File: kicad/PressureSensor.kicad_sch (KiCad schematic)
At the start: 1 part

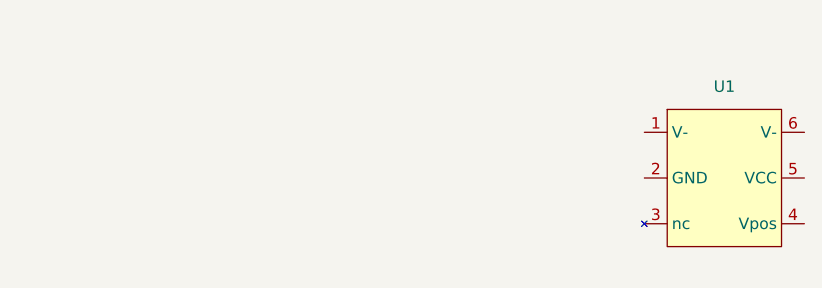
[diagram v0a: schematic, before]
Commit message: custom footprints
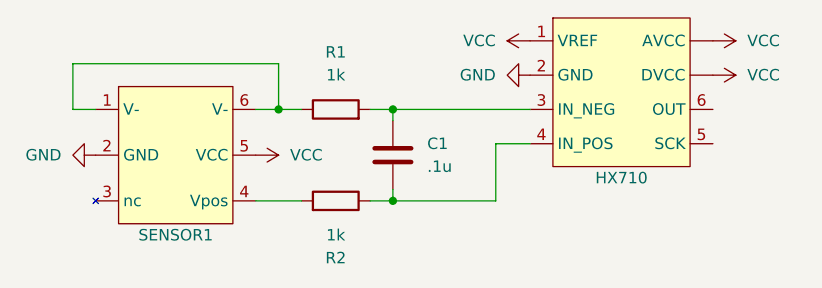
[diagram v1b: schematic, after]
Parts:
- added C1: .1u, symbol Device:C
- added HX710: ~, Package_SO:SOIC-8_5.23x5.23mm_P1.27mm, symbol New_Library:hx710
- added R1, R2: 1k, symbol Device:R
- SENSOR1: renamed from U1; footprint (none) -> Library:pressure-sensor-SOIC-6
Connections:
- net at SENSOR1.1 (V-): now also SENSOR1.6 (V-), R1.1
- net GND: now reaches SENSOR1.2 (GND)
- net GND: now also HX710.2 (GND)
- net at SENSOR1.4 (Vpos): now also R2.2
- net VCC: now reaches SENSOR1.5 (VCC)
- net VCC: now also HX710. (DVCC), HX710.1 (VREF)
- new net: C1.1, HX710.3 (IN_NEG), R1.2
- new net: C1.2, HX710.4 (IN_POS), R2.1
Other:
- moved on the sheet: SENSOR1

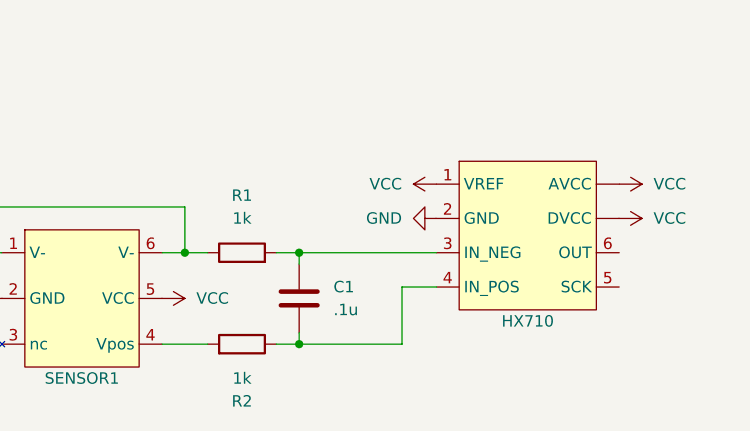
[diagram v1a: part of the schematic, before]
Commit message: schematic: improve filtering
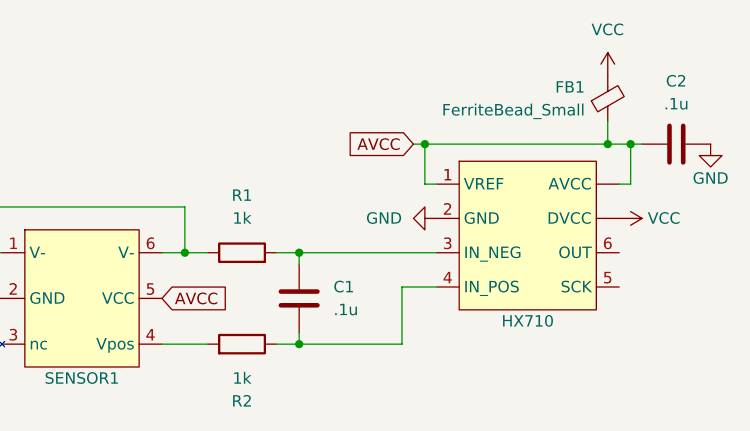
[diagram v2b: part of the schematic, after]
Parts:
- added C2: .1u, symbol Device:C
- added FB1: FerriteBead_Small, symbol Device:FerriteBead_Small
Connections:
- net GND: now also C2.2
- net VCC: now also FB1.2; no longer HX710.1 (VREF), SENSOR1.5 (VCC)
- new net AVCC: C2.1, FB1.1, HX710. (DVCC), HX710.1 (VREF), SENSOR1.5 (VCC)
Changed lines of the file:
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@@
 (kicad_sch (version 20230121) (generator eeschema)
   (paper "A4")
+  (junction (at 130.81 76.835) (diameter 0) (color 0 0 0 0)
+  )
   (junction (at 83.82 88.9) (diameter 0) (color 0 0 0 0)
   )
   (junction (at 96.52 88.9) (diameter 0) (color 0 0 0 0)
   )
+  (junction (at 110.49 76.835) (diameter 0) (color 0 0 0 0)
+  )
   (junction (at 96.52 99.06) (diameter 0) (color 0 0 0 0)
   )
+  (junction (at 133.35 76.835) (diameter 0) (color 0 0 0 0)
+  )
   (wire (pts (xy 96.52 88.9) (xy 111.76 88.9))
     (stroke (width 0) (type default))
@@
     (stroke (width 0) (type default))
   )
+  (wire (pts (xy 133.35 76.835) (xy 134.62 76.835))
+    (stroke (width 0) (type default))
+  )
+  (wire (pts (xy 130.81 74.295) (xy 130.81 76.835))
+    (stroke (width 0) (type default))
+  )
+  (wire (pts (xy 133.35 81.28) (xy 133.35 76.835))
+    (stroke (width 0) (type default))
+  )
   (wire (pts (xy 81.28 88.9) (xy 83.82 88.9))
     (stroke (width 0) (type default))
   )
+  (wire (pts (xy 130.81 76.835) (xy 110.49 76.835))
+    (stroke (width 0) (type default))
+  )
   (wire (pts (xy 96.52 90.17) (xy 96.52 88.9))
     (stroke (width 0) (type default))
@@
     (stroke (width 0) (type default))
   )
+  (wire (pts (xy 109.22 76.835) (xy 110.49 76.835))
+    (stroke (width 0) (type default))
+  )
+  (wire (pts (xy 133.35 81.28) (xy 132.08 81.28))
+    (stroke (width 0) (type default))
+  )
+  (wire (pts (xy 110.49 76.835) (xy 110.49 81.28))
+    (stroke (width 0) (type default))
+  )
   (wire (pts (xy 81.28 99.06) (xy 86.36 99.06))
     (stroke (width 0) (type default))
   )
+  (wire (pts (xy 133.35 76.835) (xy 130.81 76.835))
+    (stroke (width 0) (type default))
+  )
   (wire (pts (xy 60.96 88.9) (xy 60.96 83.82))
     (stroke (width 0) (type default))
@@
     (stroke (width 0) (type default))
   )
+  (wire (pts (xy 110.49 81.28) (xy 111.76 81.28))
+    (stroke (width 0) (type default))
+  )
   (wire (pts (xy 111.76 92.71) (xy 107.95 92.71))
     (stroke (width 0) (type default))
@@
     (stroke (width 0) (type default))
   )
-  (symbol (lib_id "power:VCC") (at 132.08 85.09 270) (unit 1)
-    (in_bom yes) (on_board yes) (dnp no) (fields_autoplaced)
-    (property "Reference" "#PWR05" (at 128.27 85.09 0)
-      (effects (font (size 1.27 1.27)) hide)
-    )
-    (property "Value" "VCC" (at 135.89 85.09 90)
-      (effects (font (size 1.27 1.27)) (justify left))
-    )
-    (property "Footprint" "" (at 132.08 85.09 0)
-      (effects (font (size 1.27 1.27)) hide)
-    )
-    (property "Datasheet" "" (at 132.08 85.09 0)
-      (effects (font (size 1.27 1.27)) hide)
-    )
-    (pin "1")
-    (instances
-      (project "PressureSensor"
-        (path "/c97cbf04-475c-40dc-8f48-12fec2eb0ee0"
-          (reference "#PWR05") (unit 1)
-        )
-      )
+  (global_label "AVCC" (shape input) (at 109.22 76.835 180) (fields_autoplaced)
+    (effects (font (size 1.27 1.27)) (justify right))
+    (property "Intersheetrefs" "${INTERSHEET_REFS}" (at 101.5176 76.835 0)
+      (effects (font (size 1.27 1.27)) (justify right) hide)
+    )
+  )
+  (global_label "AVCC" (shape input) (at 81.28 93.98 0) (fields_autoplaced)
+    (effects (font (size 1.27 1.27)) (justify left))
+    (property "Intersheetrefs" "${INTERSHEET_REFS}" (at 88.9824 93.98 0)
+      (effects (font (size 1.27 1.27)) (justify left) hide)
     )
   )
@@
     )
   )
-  (symbol (lib_id "power:VCC") (at 111.76 81.28 90) (unit 1)
-    (in_bom yes) (on_board yes) (dnp no) (fields_autoplaced)
-    (property "Reference" "#PWR06" (at 115.57 81.28 0)
-      (effects (font (size 1.27 1.27)) hide)
-    )
-    (property "Value" "VCC" (at 107.95 81.28 90)
-      (effects (font (size 1.27 1.27)) (justify left))
-    )
-    (property "Footprint" "" (at 111.76 81.28 0)
-      (effects (font (size 1.27 1.27)) hide)
-    )
-    (property "Datasheet" "" (at 111.76 81.28 0)
-      (effects (font (size 1.27 1.27)) hide)
-    )
-    (pin "1")
-    (instances
-      (project "PressureSensor"
-        (path "/c97cbf04-475c-40dc-8f48-12fec2eb0ee0"
-          (reference "#PWR06") (unit 1)
+  (symbol (lib_id "Device:C") (at 138.43 76.835 90) (unit 1)
+    (in_bom yes) (on_board yes) (dnp no) (fields_autoplaced)
+    (property "Reference" "C2" (at 138.43 69.85 90)
+      (effects (font (size 1.27 1.27)))
+    )
+    (property "Value" ".1u" (at 138.43 72.39 90)
+      (effects (font (size 1.27 1.27)))
+    )
+    (property "Footprint" "" (at 142.24 75.8698 0)
+      (effects (font (size 1.27 1.27)) hide)
+    )
+    (property "Datasheet" "~" (at 138.43 76.835 0)
+      (effects (font (size 1.27 1.27)) hide)
+    )
+    (pin "1")
+    (pin "2")
+    (instances
+      (project "PressureSensor"
+        (path "/c97cbf04-475c-40dc-8f48-12fec2eb0ee0"
+          (reference "C2") (unit 1)
         )
       )
@@
     )
   )
-  (symbol (lib_id "power:VCC") (at 132.08 81.28 270) (unit 1)
-    (in_bom yes) (on_board yes) (dnp no) (fields_autoplaced)
-    (property "Reference" "#PWR04" (at 128.27 81.28 0)
-      (effects (font (size 1.27 1.27)) hide)
-    )
-    (property "Value" "VCC" (at 135.89 81.28 90)
+  (symbol (lib_id "power:VCC") (at 130.81 69.215 0) (unit 1)
+    (in_bom yes) (on_board yes) (dnp no) (fields_autoplaced)
+    (property "Reference" "#PWR04" (at 130.81 73.025 0)
+      (effects (font (size 1.27 1.27)) hide)
+    )
+    (property "Value" "VCC" (at 130.81 64.135 0)
+      (effects (font (size 1.27 1.27)))
+    )
+    (property "Footprint" "" (at 130.81 69.215 0)
+      (effects (font (size 1.27 1.27)) hide)
+    )
+    (property "Datasheet" "" (at 130.81 69.215 0)
+      (effects (font (size 1.27 1.27)) hide)
+    )
+    (pin "1")
+    (instances
+      (project "PressureSensor"
+        (path "/c97cbf04-475c-40dc-8f48-12fec2eb0ee0"
+          (reference "#PWR04") (unit 1)
+        )
+      )
+    )
+  )
+  (symbol (lib_id "power:VCC") (at 132.08 85.09 270) (unit 1)
+    (in_bom yes) (on_board yes) (dnp no)
+    (property "Reference" "#PWR05" (at 128.27 85.09 0)
+      (effects (font (size 1.27 1.27)) hide)
+    )
+    (property "Value" "VCC" (at 135.255 85.09 90)
       (effects (font (size 1.27 1.27)) (justify left))
     )
-    (property "Footprint" "" (at 132.08 81.28 0)
-      (effects (font (size 1.27 1.27)) hide)
-    )
-    (property "Datasheet" "" (at 132.08 81.28 0)
-      (effects (font (size 1.27 1.27)) hide)
-    )
-    (pin "1")
-    (instances
-      (project "PressureSensor"
-        (path "/c97cbf04-475c-40dc-8f48-12fec2eb0ee0"
-          (reference "#PWR04") (unit 1)
+    (property "Footprint" "" (at 132.08 85.09 0)
+      (effects (font (size 1.27 1.27)) hide)
+    )
+    (property "Datasheet" "" (at 132.08 85.09 0)
+      (effects (font (size 1.27 1.27)) hide)
+    )
+    (pin "1")
+    (instances
+      (project "PressureSensor"
+        (path "/c97cbf04-475c-40dc-8f48-12fec2eb0ee0"
+          (reference "#PWR05") (unit 1)
+        )
+      )
+    )
+  )
+  (symbol (lib_id "Device:FerriteBead_Small") (at 130.81 71.755 0) (mirror x) (unit 1)
+    (in_bom yes) (on_board yes) (dnp no)
+    (property "Reference" "FB1" (at 128.27 70.5231 0)
+      (effects (font (size 1.27 1.27)) (justify right))
+    )
+    (property "Value" "FerriteBead_Small" (at 128.27 73.0631 0)
+      (effects (font (size 1.27 1.27)) (justify right))
+    )
+    (property "Footprint" "" (at 129.032 71.755 90)
+      (effects (font (size 1.27 1.27)) hide)
+    )
+    (property "Datasheet" "~" (at 130.81 71.755 0)
+      (effects (font (size 1.27 1.27)) hide)
+    )
+    (pin "1")
+    (pin "2")
+    (instances
+      (project "PressureSensor"
+        (path "/c97cbf04-475c-40dc-8f48-12fec2eb0ee0"
+          (reference "FB1") (unit 1)
         )
       )
@@
         (path "/c97cbf04-475c-40dc-8f48-12fec2eb0ee0"
           (reference "R1") (unit 1)
+        )
+      )
+    )
+  )
+  (symbol (lib_id "power:GND") (at 142.24 76.835 0) (unit 1)
+    (in_bom yes) (on_board yes) (dnp no)
+    (property "Reference" "#PWR07" (at 142.24 83.185 0)
+      (effects (font (size 1.27 1.27)) hide)
+    )
+    (property "Value" "GND" (at 142.24 80.645 0)
+      (effects (font (size 1.27 1.27)))
+    )
+    (property "Footprint" "" (at 142.24 76.835 0)
+      (effects (font (size 1.27 1.27)) hide)
+    )
+    (property "Datasheet" "" (at 142.24 76.835 0)
+      (effects (font (size 1.27 1.27)) hide)
+    )
+    (pin "1")
+    (instances
+      (project "PressureSensor"
+        (path "/c97cbf04-475c-40dc-8f48-12fec2eb0ee0"
+          (reference "#PWR07") (unit 1)
         )
       )
@@
         )
       )
-    )
-  )
-  (symbol (lib_id "power:VCC") (at 81.28 93.98 270) (unit 1)
-    (in_bom yes) (on_board yes) (dnp no) (fields_autoplaced)
-    (property "Reference" "#PWR02" (at 77.47 93.98 0)
-      (effects (font (size 1.27 1.27)) hide)
-    )
-    (property "Value" "VCC" (at 85.09 93.98 90)
-      (effects (font (size 1.27 1.27)) (justify left))
-    )
-    (property "Footprint" "" (at 81.28 93.98 0)
-      (effects (font (size 1.27 1.27)) hide)
-    )
-    (property "Datasheet" "" (at 81.28 93.98 0)
-      (effects (font (size 1.27 1.27)) hide)
-    )
-    (pin "1")
-    (instances
-      (project "PressureSensor"
-        (path "/c97cbf04-475c-40dc-8f48-12fec2eb0ee0"
-          (reference "#PWR02") (unit 1)
-        )
-      )

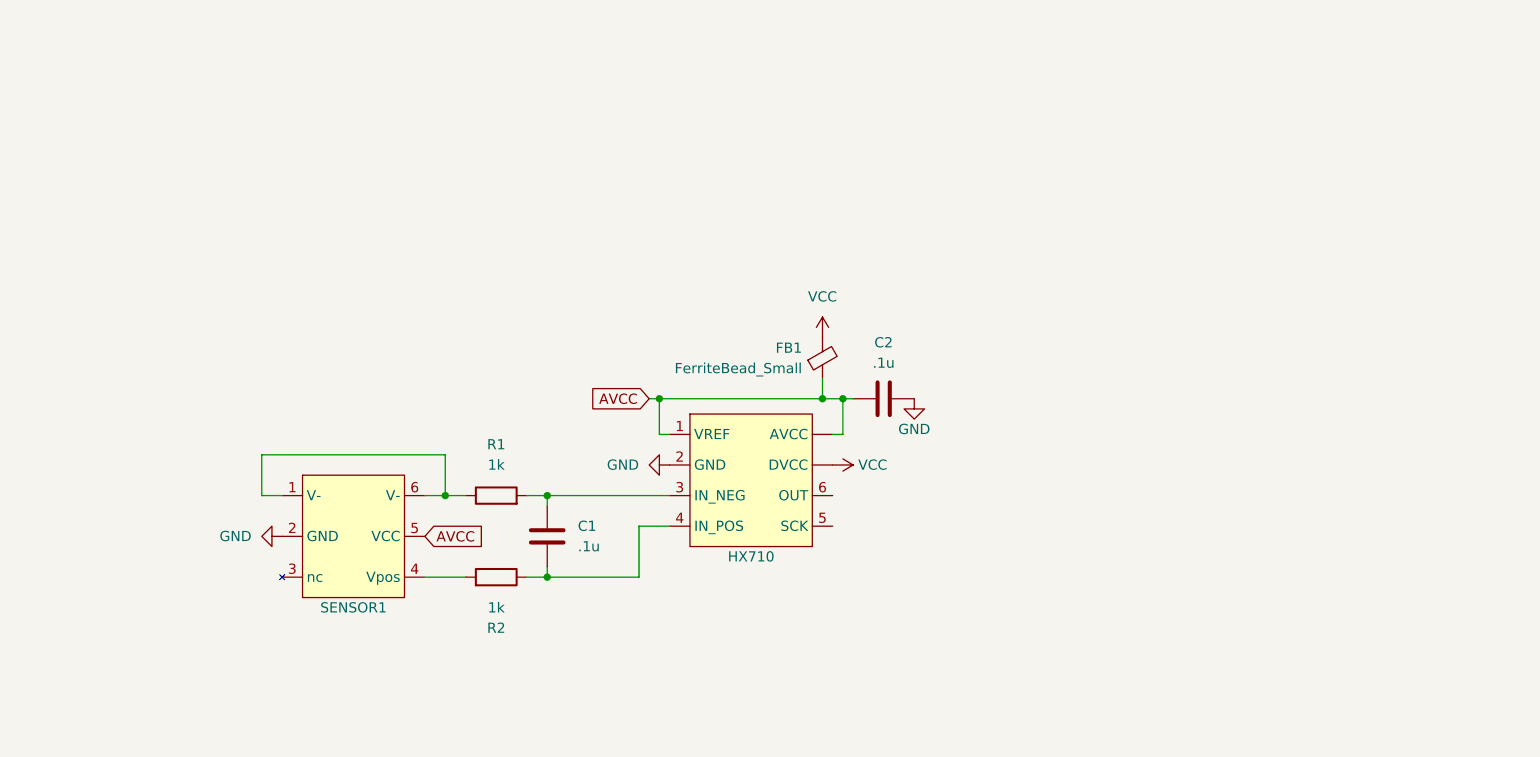
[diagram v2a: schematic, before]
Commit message: schematic: all major components
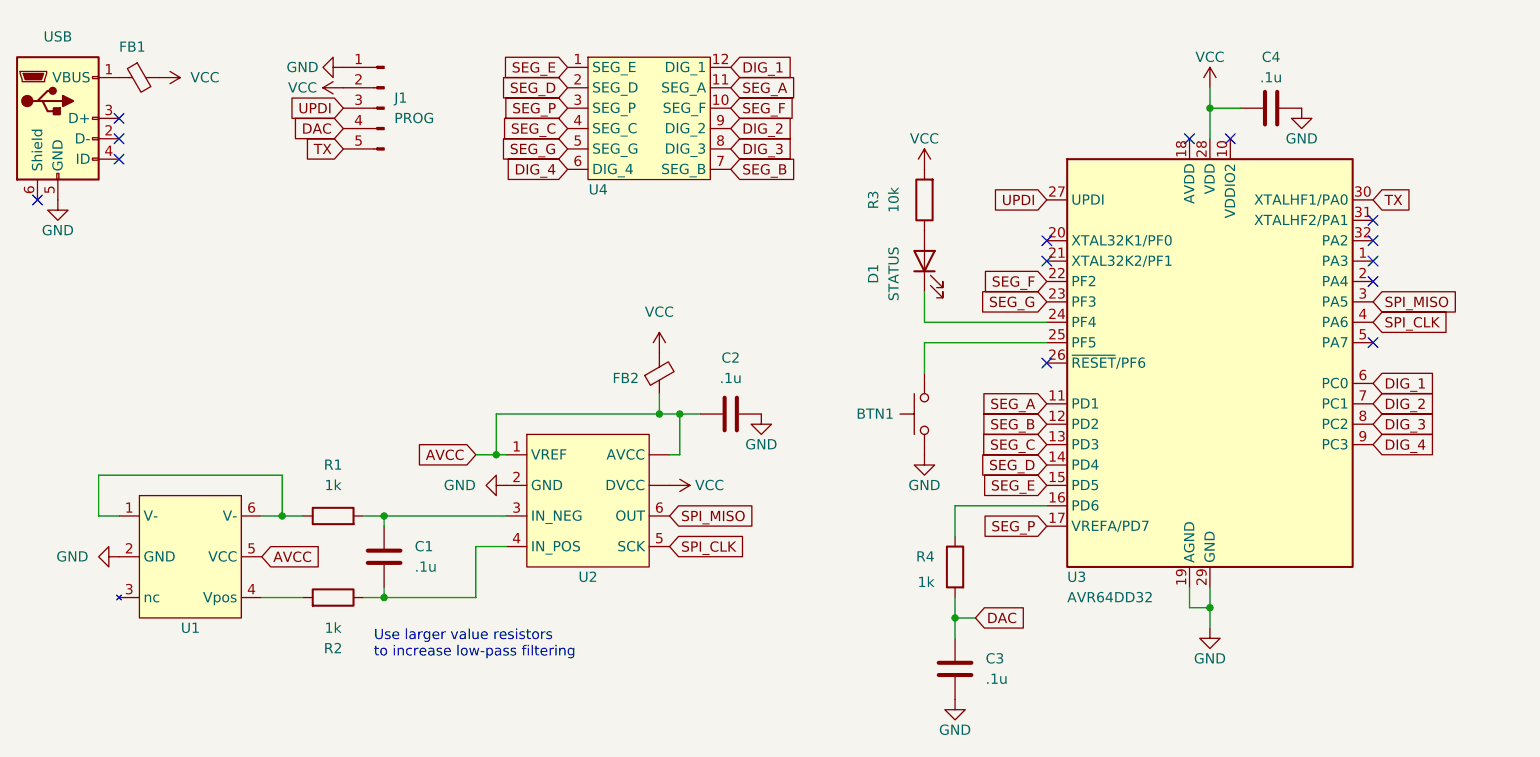
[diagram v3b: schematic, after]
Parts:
- added BTN1: SW_Push, symbol Switch:SW_Push
- added C3, C4: .1u, symbol Device:C
- added D1: STATUS, symbol Device:LED
- added FB1: FerriteBead_Small, symbol Device:FerriteBead_Small
- added J1: PROG, symbol Connector:Conn_01x05_Pin
- added R3: 10k, symbol Device:R
- added R4: 1k, symbol Device:R
- added U3: AVR64DD32, Package_QFP:TQFP-32_7x7mm_P0.8mm, symbol MCU_Microchip_AVR_Dx:AVR64DB32x-xPT
- added U4: ~, symbol New_Library:display
- added USB: USB_B_Micro, symbol Connector:USB_B_Micro
- renumbered FB1 to FB2, SENSOR1 to U1, HX710 to U2
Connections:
- net GND: now also BTN1.2, C3.2, C4.2, J1.1 (Pin_1), U3.19 (AGND), U3.29 (GND), USB.5 (GND)
- net VCC: now also C4.1, FB1.2, J1.2 (Pin_2), R3.2, U3.28 (VDD)
- net SPI_CLK: now reaches U2.5 (SCK)
- net SPI_CLK: now also U3.4 (PA6)
- net SPI_MISO: now reaches U2.6 (OUT)
- net SPI_MISO: now also U3.3 (PA5)
- new net: D1.2 (A), R3.1
- new net: FB1.1, USB.1 (VBUS)
- new net: R4.1, U3.16 (PD6)
- new net: D1.1 (K), U3.24 (PF4)
- new net: BTN1.1, U3.25 (PF5)
- new net DAC: C3.1, J1.4 (Pin_4), R4.2
- new net DIG_1: U3.6 (PC0), U4.12 (DIG_1)
- new net DIG_2: U3.7 (PC1), U4.9 (DIG_2)
- new net DIG_3: U3.8 (PC2), U4.8 (DIG_3)
- new net DIG_4: U3.9 (PC3), U4.6 (DIG_4)
- new net SEG_A: U3.11 (PD1), U4.11 (SEG_A)
- new net SEG_B: U3.12 (PD2), U4.7 (SEG_B)
- new net SEG_C: U3.13 (PD3), U4.4 (SEG_C)
- new net SEG_D: U3.14 (PD4), U4.2 (SEG_D)
- new net SEG_E: U3.15 (PD5), U4.1 (SEG_E)
- new net SEG_F: U3.22 (PF2), U4.10 (SEG_F)
- new net SEG_G: U3.23 (PF3), U4.5 (SEG_G)
- new net SEG_P: U3.17 (VREFA/PD7), U4.3 (SEG_P)
- new net TX: J1.5 (Pin_5), U3.30 (XTALHF1/PA0)
- new net UPDI: J1.3 (Pin_3), U3.27 (UPDI)
- no-connect marks 0 -> 14
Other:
- note added: "Use larger value resistors to increase low-pass filtering"
- moved on the sheet: C1, C2, FB2, R1, R2, U1, U2

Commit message: improve HX710 symbol
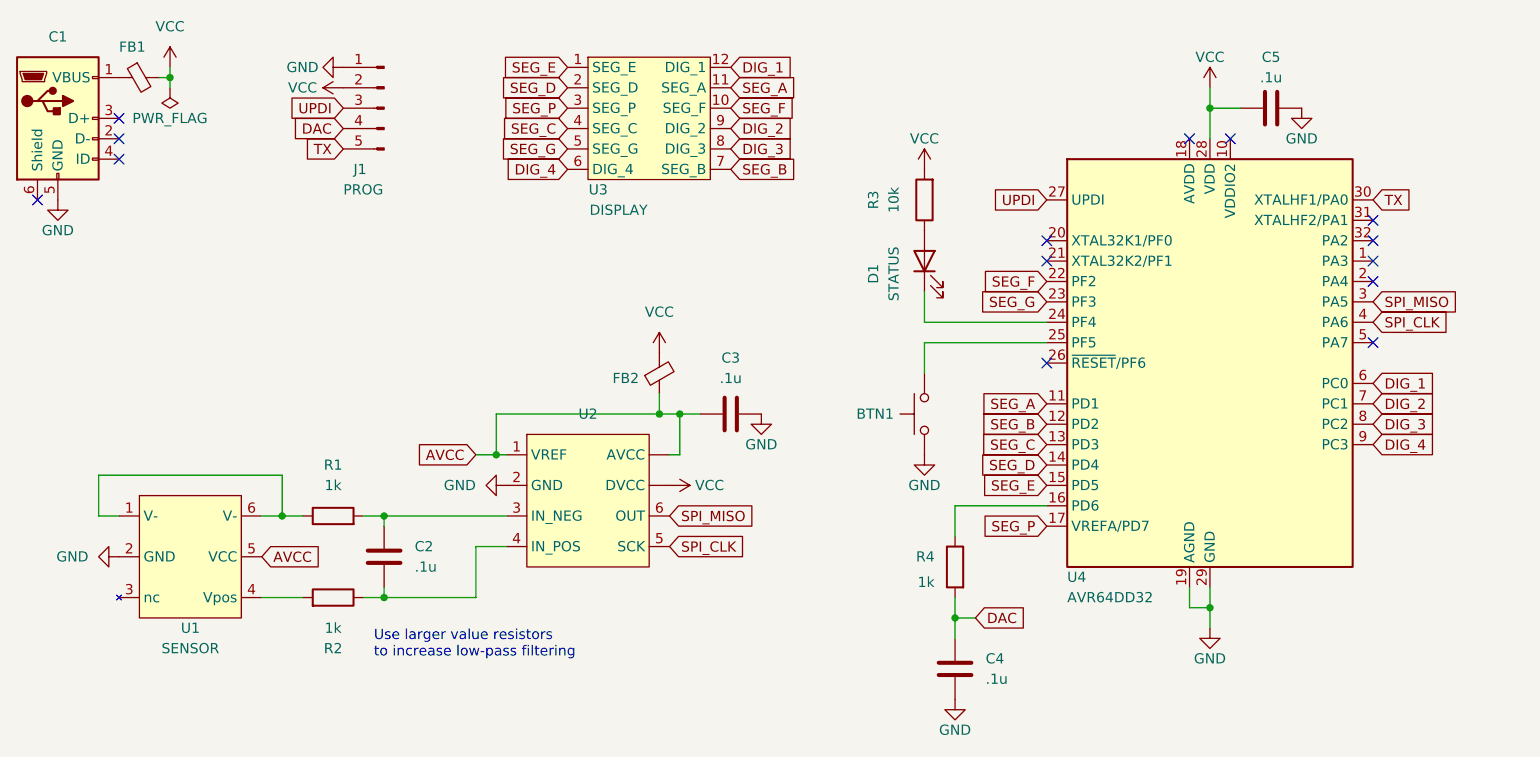
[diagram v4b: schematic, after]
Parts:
- U1: value ~ -> SENSOR
- U2: footprint Package_SO:SOIC-8_5.23x5.23mm_P1.27mm -> (none)
- U3: renamed from U4; value ~ -> DISPLAY
- renumbered USB to C1, C1 to C2, C2 to C3, C3 to C4, C4 to C5, U3 to U4

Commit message: update PCB layout
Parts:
- BTN1: footprint (none) -> Button_Switch_THT:SW_PUSH_6mm_H5mm
- C1: footprint (none) -> Connector_USB:USB_Micro-B_Amphenol_10118193-0001LF_Horizontal
- C2, C3, C4, C5: footprint (none) -> Capacitor_SMD:C_0805_2012Metric_Pad1.18x1.45mm_HandSolder
- D1: footprint (none) -> LED_SMD:LED_0805_2012Metric_Pad1.15x1.40mm_HandSolder
- FB1, FB2, R1, R2, R3, R4: footprint (none) -> Resistor_SMD:R_0805_2012Metric_Pad1.20x1.40mm_HandSolder
- J1: footprint (none) -> Connector_PinHeader_2.54mm:PinHeader_1x05_P2.54mm_Vertical
- U2: value ~ -> HX710; footprint (none) -> Package_SO:SSOP-8_3.9x5.05mm_P1.27mm
- U3: footprint (none) -> Library:7_seg_display_DIP12
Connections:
- net AVCC: now also U2.8 (AVCC); no longer U2. (DVCC)
- net VCC: now also U2.7 (DVCC); no longer U2. (DVCC)
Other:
- moved on the sheet: BTN1, C4, C5, D1, R3, R4, U4
